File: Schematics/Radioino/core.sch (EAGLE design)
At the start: 16 parts

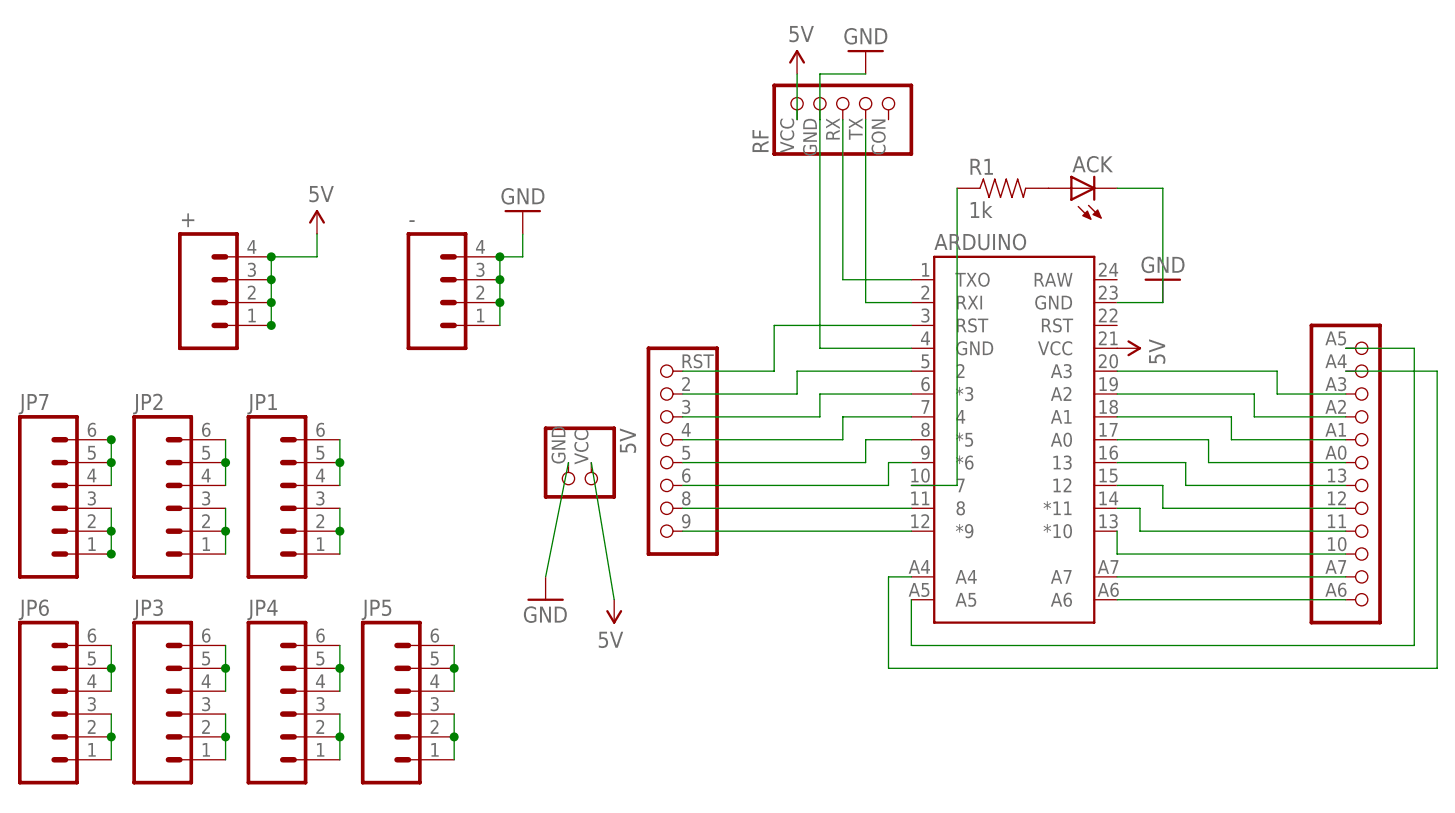
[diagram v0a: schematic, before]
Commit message: New board Added the "program" button on the board
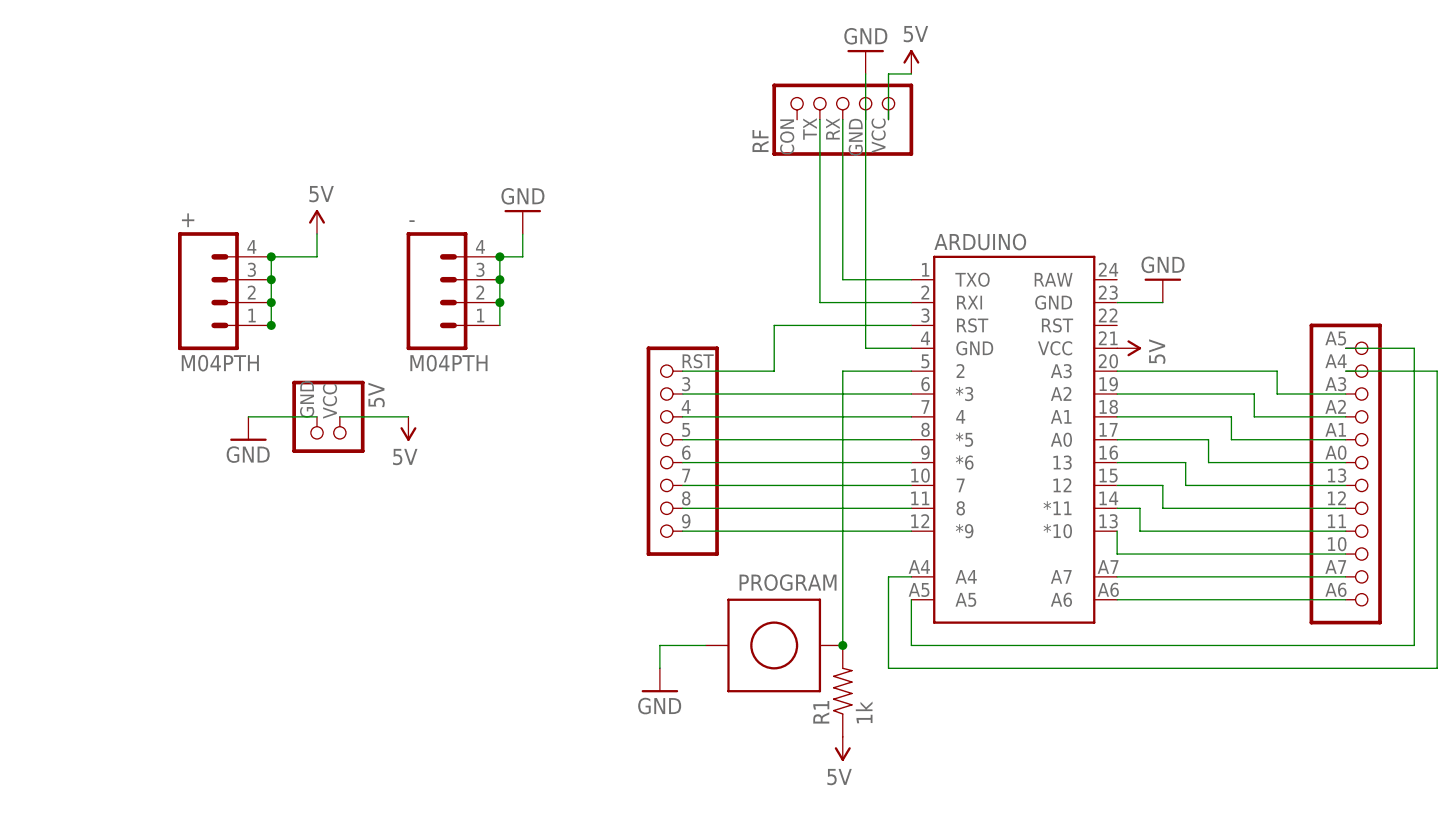
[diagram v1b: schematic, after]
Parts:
- removed ACK: (no value), led:LED3MM
- removed JP1, JP2, JP3, JP4, JP5, JP6, JP7: (no value), SparkFun-Connectors:M06POGOPIN_HOLES_ONLY
- added PROGRAM: PUSHBUTTON, jalf:PUSHBUTTON
- +, -: value (none) -> M04PTH; device SparkFun-Connectors:M04PTH -> jalf:M04PTH
- R1: device SparkFun-Resistors:RESISTORPTH-1/4W -> SparkFun-Resistors:RESISTORPTH-1/4W-VERT
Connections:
- removed net N$15 (its old number): ARDUINO.*6, U$2.3
- removed net N$16 (its old number): ARDUINO.*5, U$2.4
- removed net N$24: ACK.A, R1.2
- removed net N$25: JP7.1, JP7.2, JP7.3
- removed net N$26: JP2.1, JP2.2, JP2.3
- removed net N$27: JP1.1, JP1.2, JP1.3
- removed net N$28: JP6.1, JP6.2, JP6.3
- removed net N$29: JP3.1, JP3.2, JP3.3
- removed net N$30: JP4.1, JP4.2, JP4.3
- removed net N$31: JP5.1, JP5.2, JP5.3
- removed net N$32: JP7.4, JP7.5, JP7.6
- removed net N$33: JP2.4, JP2.5, JP2.6
- removed net N$34: JP1.4, JP1.5, JP1.6
- removed net N$35: JP5.4, JP5.5, JP5.6
- removed net N$36: JP4.4, JP4.5, JP4.6
- removed net N$37: JP3.4, JP3.5, JP3.6
- removed net N$38: JP6.4, JP6.5, JP6.6
- new net N$14: ARDUINO.RXI, RF.2
- new net N$18: ARDUINO.*6, U$2.4
- net 5V: now also R1.1, RF.5; no longer RF.1
- net GND: now also PROGRAM.P$1, RF.4; no longer ACK.C, RF.2
- net N$17: now also ARDUINO.7, U$2.3; no longer ARDUINO.4, U$2.5
- net N$19: now also ARDUINO.*5, U$2.5; no longer ARDUINO.RXI, RF.4
- net N$20: now also ARDUINO.4; no longer ARDUINO.*3
- net N$21: now also ARDUINO.*3; no longer ARDUINO.2
- net N$23: now also ARDUINO.2, PROGRAM.P$2, R1.2; no longer ARDUINO.7, R1.1
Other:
- moved on the sheet: 5V, R1
